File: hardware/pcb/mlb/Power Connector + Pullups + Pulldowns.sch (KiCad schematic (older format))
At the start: 48 parts, among them J12 Power & Video Connector, J14B EDGE CONN BOT, J14T EDGE CONN TOP

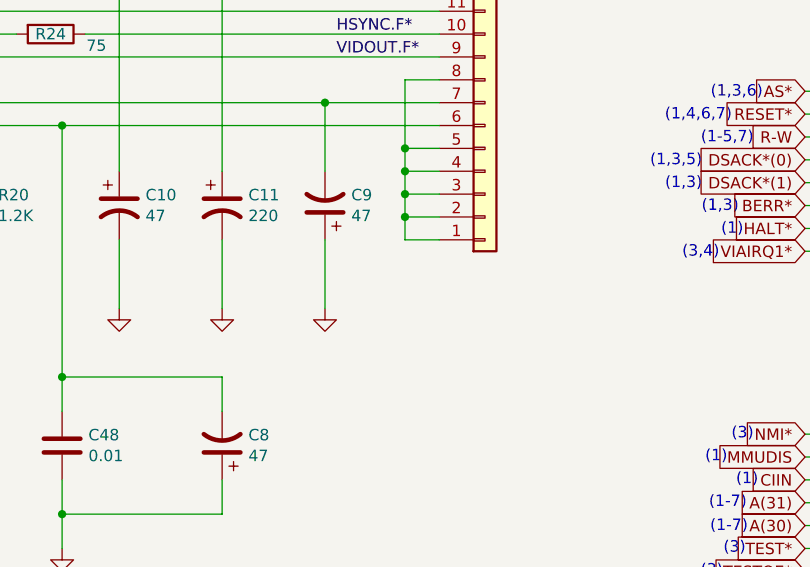
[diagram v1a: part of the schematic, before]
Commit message: Fix missing GND.
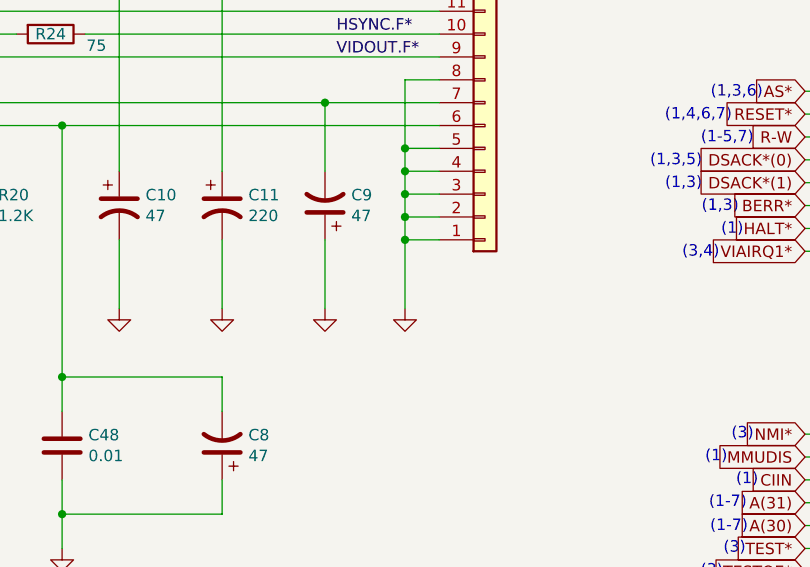
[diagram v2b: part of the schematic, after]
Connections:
- wire segments 216 -> 217
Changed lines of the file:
@@
 Text Notes 10630 4885 0    50   ~ 0
 (1)
+$Comp
+L power:GND #PWR?
+U 1 1 5F4D59A5
+P 5450 3600
+F 0 "#PWR?" H 5450 3350 50  0001 C CNN
+F 1 "GND" H 5455 3427 50  0001 C CNN
+F 2 "" H 5450 3600 50  0001 C CNN
+F 3 "" H 5450 3600 50  0001 C CNN
+	1    5450 3600
+	1    0    0    -1
+$EndComp
+Wire Wire Line
+	5450 3300 5450 3600
+Connection ~ 5450 3300
 $EndSCHEMATC

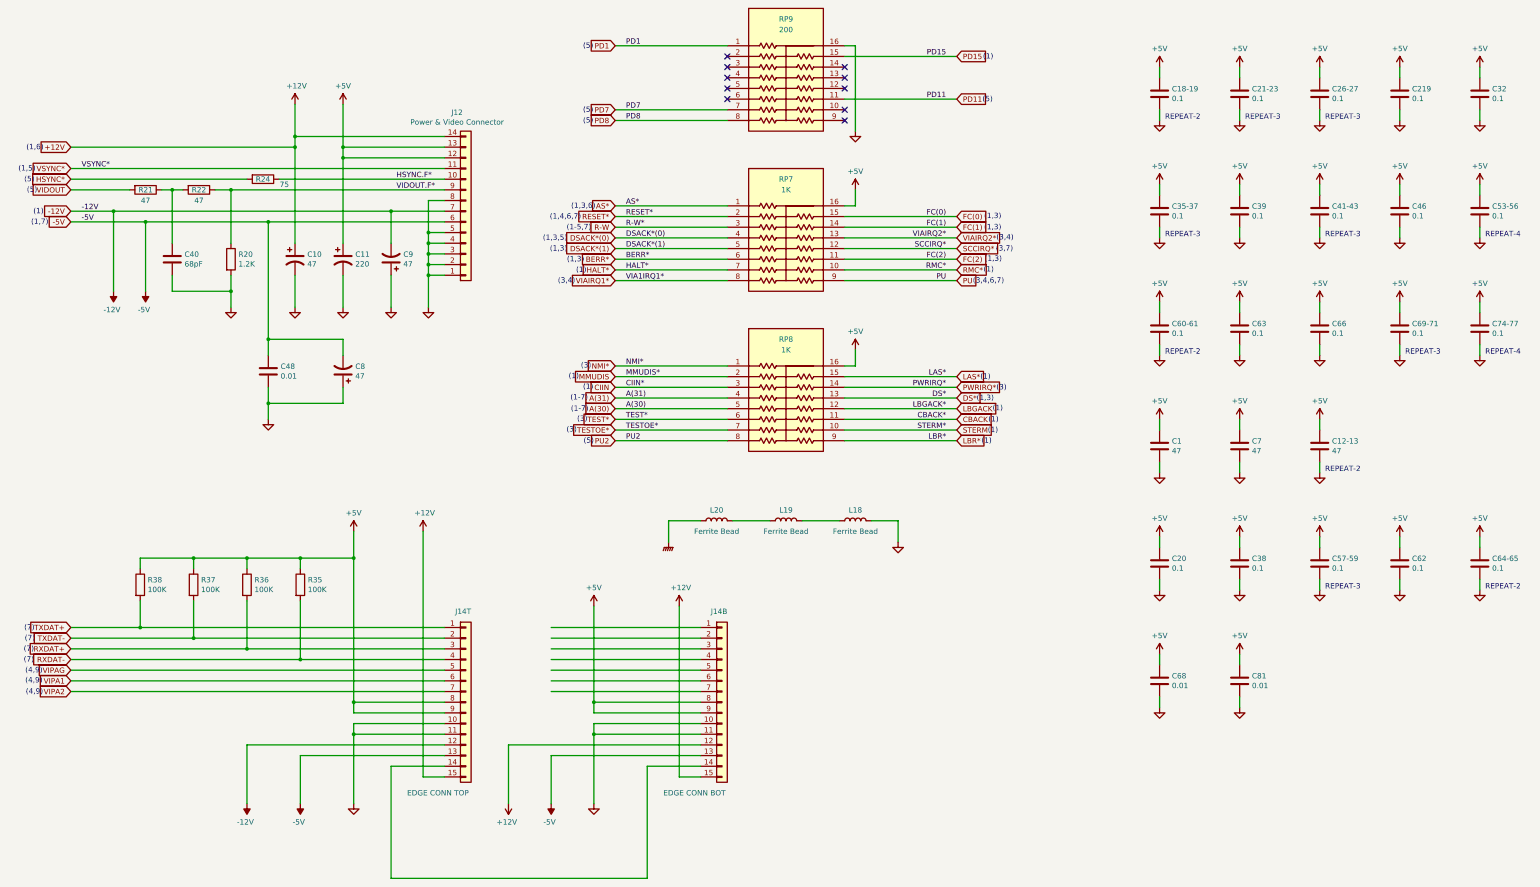
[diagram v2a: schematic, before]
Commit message: Fix errors found in review of the Macintosh SE/30 schematic redraw.
Page 1:

* DSACK*(0:1) (syntax)
* R-W* (inconsistent syntax)
* IPL different syntax
* PDS 38, C16M not grounded
* PDS 39, should be grounded

Page 2:

* RAAF*(8), RABF*(9), RAAF*(10), RABF*(10) (syntax)
* RCMUX* (syntax)
* ROM* missing page 3 indicator
* ROMSIMM1 GND 10, 30, 64
* ROMSIMM1 Incorrect +5V lines
* ROMSIMM1 Confusing bus line drawing angles makes connections look
  duplicated

Page 3:

* VIAIRQ2* (syntax)
* VIAIRQ1N (syntax, on GLUE template)
* SCCRD* (syntax)

Page 4:

* VIA template, RS0, RS1, RS2, RS3 erroneously written as R50, R51,
  R52, R53
* V1PB7 erroneously written as VIPB7
* RTC-D erroneously written as RTC-O
* V1PA0, V1PA1, V1PA2 erroneously written as VIPA0, VIPA1, VIPA2
* warning: additional label BATT not present
* UL11 ADB template, P5 erroneously written as P2
* ADBO erroneously written as ADB0
* SNDINT* erroneously written as SNTINT*

Page 5:

* HSYNC* on UG7 (syntax)
* UJ6 confusing bus line makes signals look duplicated
* Video ROM UK6 not labeled with reference designator (already inside
  KiCad file, stale PDF?)
* VIDS4, VIDS3, VIDS2, VIDS1, VIDS0 erroneously written a VID54,
  VID53, VID53, VID51, VID50
* R-W* alternate page reference erroneously written as RW*
* 74F253 template, G erroneously labeled as GND
* 74F253 template, missing second G enable pin
* style: C0 in 74F253 template should not be C0(GND)
* warning: UA8 ALTVID line could have another label close to the chip

Page 6:

* warning: On SWIM, WRDATA could have label WR*
* DB25 connector: DP*, DB0*, DB1*, DB2*, DB3*, DB4*, DB5*, DB6*, DB7*
  (syntax)
* J8 Ribbon Connector: Missing +12V on 13, 15, 17, 19
* J6 DB-19: Missing +12V-DSK on 7, 8
* warning: missing RDDATA.F additional label near J6 DB-19 pin 18
* warning: missing WRITE.F additional label near J6 DB-19 pin 19
* warning: confusing bus line layout on 53C80 looks like duplicate
  wiring

Page 7:

* RXDA+ erroneously written as RXDB+
* HSKOA erroneo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
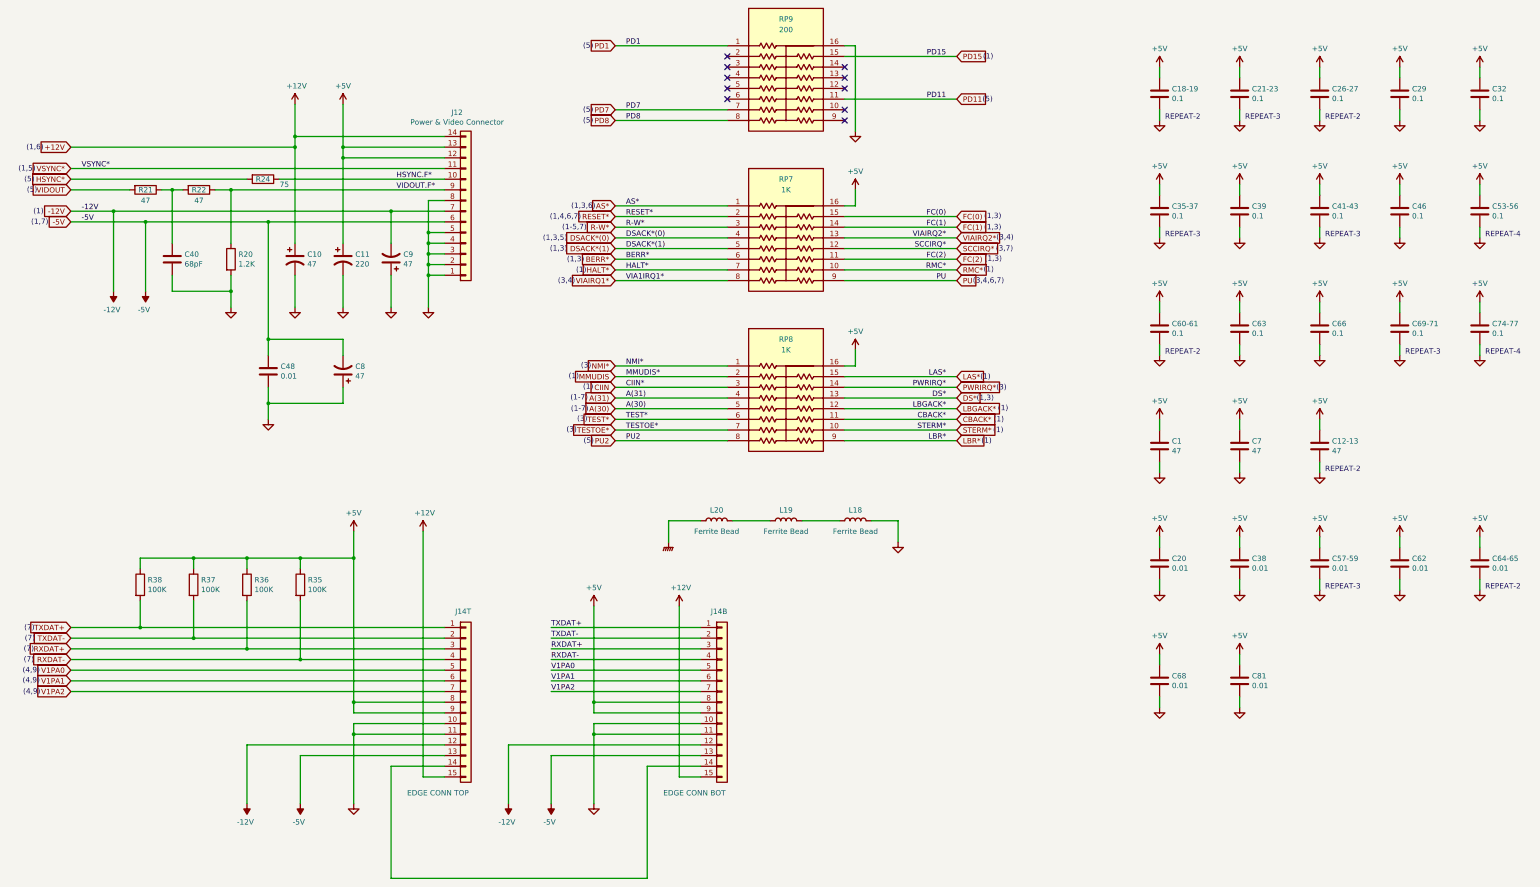
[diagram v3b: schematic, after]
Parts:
- C20, C38, C57-59, C62, C64-65: value 0.1 -> 0.01
- renumbered C219 to C29
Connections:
- net VIPA1 is gone; now on net V1PA1: J14T.6 (Pin_6)
- net VIPA2 is gone; now on net V1PA2: J14T.7 (Pin_7)
- net VIPAG is gone; now on net V1PA0: J14T.5 (Pin_5)
- net +12V: no longer J14B.12 (Pin_12)
- net -12V: now also J14B.12 (Pin_12)
- net RXDAT+: now also J14B.3 (Pin_3)
- net RXDAT-: now also J14B.4 (Pin_4)
- net TXDAT+: now also J14B.1 (Pin_1)
- net TXDAT-: now also J14B.2 (Pin_2)
- net V1PA0: now reaches J14B.5 (Pin_5)
- net V1PA1: now reaches J14B.6 (Pin_6)
- net V1PA2: now reaches J14B.7 (Pin_7)
- net CBACK renamed CBACK*
- net LBGACK renamed LBGACK*
- net R-W renamed R-W*
- net STERM renamed STERM*
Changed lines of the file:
@@
 R-W*
 Text GLabel 7200 2850 0    50   Input ~ 0
-R-W
+R-W*
 Wire Wire Line
 	8250 2950 7200 2950
@@
 STERM*
 Text GLabel 10400 4750 2    50   Input ~ 0
-STERM
+STERM*
 Wire Wire Line
 	9350 4650 10400 4650
@@
 CBACK*
 Text GLabel 10400 4650 2    50   Input ~ 0
-CBACK
+CBACK*
 Wire Wire Line
 	9350 4550 10400 4550
 Text Label 10300 4550 2    50   ~ 0
 LBGACK*
-Text GLabel 10400 4550 2    50   Input ~ 0
-LBGACK
 Wire Wire Line
 	9350 4450 10400 4450
@@
 RXDAT-
 Text GLabel 2100 7000 0    50   Input ~ 0
-VIPAG
+V1PA0
 Text GLabel 2100 7100 0    50   Input ~ 0
-VIPA1
+V1PA1
 Text GLabel 2100 7200 0    50   Input ~ 0
-VIPA2
+V1PA2
 Wire Wire Line
 	5600 8000 5400 8000
@@
 $EndComp
 $Comp
-L power:+12V #PWR?
-U 1 1 5F8BC6F1
-P 6200 8250
-F 0 "#PWR?" H 6200 8100 50  0001 C CNN
-F 1 "+12V" H 6215 8423 50  0000 C CNN
-F 2 "" H 6200 8250 50  0001 C CNN
-F 3 "" H 6200 8250 50  0001 C CNN
-	1    6200 8250
-	-1   0    0    1
-$EndComp
-$Comp
 L Device:C C18-19
 U 1 1 5F8EE69A
@@
 $EndComp
 Text Notes 13850 1850 0    50   ~ 0
-REPEAT-3
-$Comp
-L Device:C C219
+REPEAT-2
+$Comp
+L Device:C C29
 U 1 1 5F92D6F5
 P 14550 1600
-F 0 "C219" H 14665 1646 50  0000 L CNN
+F 0 "C29" H 14665 1646 50  0000 L CNN
 F 1 "0.1" H 14665 1555 50  0000 L CNN
 F 2 "" H 14588 1450 50  0001 C CNN
@@
 P 12300 6000
 F 0 "C20" H 12415 6046 50  0000 L CNN
-F 1 "0.1" H 12415 5955 50  0000 L CNN
+F 1 "0.01" H 12415 5955 50  0000 L CNN
 F 2 "" H 12338 5850 50  0001 C CNN
 F 3 "~" H 12300 6000 50  0001 C CNN
@@
 P 13050 6000
 F 0 "C38" H 13165 6046 50  0000 L CNN
-F 1 "0.1" H 13165 5955 50  0000 L CNN
+F 1 "0.01" H 13165 5955 50  0000 L CNN
 F 2 "" H 13088 5850 50  0001 C CNN
 F 3 "~" H 13050 6000 50  0001 C CNN
@@
 P 13800 6000
 F 0 "C57-59" H 13915 6046 50  0000 L CNN
-F 1 "0.1" H 13915 5955 50  0000 L CNN
+F 1 "0.01" H 13915 5955 50  0000 L CNN
 F 2 "" H 13838 5850 50  0001 C CNN
 F 3 "~" H 13800 6000 50  0001 C CNN
@@
 P 14550 6000
 F 0 "C62" H 14665 6046 50  0000 L CNN
-F 1 "0.1" H 14665 5955 50  0000 L CNN
+F 1 "0.01" H 14665 5955 50  0000 L CNN
 F 2 "" H 14588 5850 50  0001 C CNN
 F 3 "~" H 14550 6000 50  0001 C CNN
@@
 P 15300 6000
 F 0 "C64-65" H 15415 6046 50  0000 L CNN
-F 1 "0.1" H 15415 5955 50  0000 L CNN
+F 1 "0.01" H 15415 5955 50  0000 L CNN
 F 2 "" H 15338 5850 50  0001 C CNN
 F 3 "~" H 15300 6000 50  0001 C CNN
@@
 Text Notes 1755 6935 2    50   ~ 0
 (7)
-Text Notes 1835 7035 2    50   ~ 0
+Text Notes 1810 7035 2    50   ~ 0
 (4,9)
-Text Notes 1835 7130 2    50   ~ 0
+Text Notes 1810 7130 2    50   ~ 0
 (4,9)
-Text Notes 1840 7235 2    50   ~ 0
+Text Notes 1815 7235 2    50   ~ 0
 (4,9)
 Text Notes 6995 1185 2    50   ~ 0
@@
 Text Notes 6880 2785 2    50   ~ 0
 (1,4,6,7)
-Text Notes 6975 2885 2    50   ~ 0
+Text Notes 6933 2884 2    50   ~ 0
 (1-5,7)
 Text Notes 6750 2985 2    50   ~ 0
@@
 Text Notes 10585 4485 0    50   ~ 0
 (1,3)
-Text Notes 10735 4580 0    50   ~ 0
+Text Notes 10785 4580 0    50   ~ 0
 (1)
-Text Notes 10695 4685 0    50   ~ 0
+Text Notes 10745 4685 0    50   ~ 0
 (1)
-Text Notes 10690 4785 0    50   ~ 0
+Text Notes 10740 4785 0    50   ~ 0
 (1)
 Text Notes 10630 4885 0    50   ~ 0
@@
 	5450 3300 5450 3600
 Connection ~ 5450 3300
+Text Label 6600 6600 0    50   ~ 0
+TXDAT+
+Text Label 6600 6700 0    50   ~ 0
+TXDAT-
+Text Label 6600 6800 0    50   ~ 0
+RXDAT+
+Text Label 6600 6900 0    50   ~ 0
+RXDAT-
+Text Label 6600 7000 0    50   ~ 0
+V1PA0
+Text Label 6600 7100 0    50   ~ 0
+V1PA1
+Text Label 6600 7200 0    50   ~ 0
+V1PA2
+$Comp
+L power:-12V #PWR?
+U 1 1 607DCB16
+P 6200 8250
+F 0 "#PWR?" H 6200 8350 50  0001 C CNN
+F 1 "-12V" H 6215 8423 50  0000 C CNN
+F 2 "" H 6200 8250 50  0001 C CNN
+F 3 "" H 6200 8250 50  0001 C CNN
+	1    6200 8250
+	-1   0    0    1
+$EndComp
+Text GLabel 10400 4550 2    50   Input ~ 0
+LBGACK*
 $EndSCHEMATC
